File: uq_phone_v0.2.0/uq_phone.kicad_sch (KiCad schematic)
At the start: 0 parts

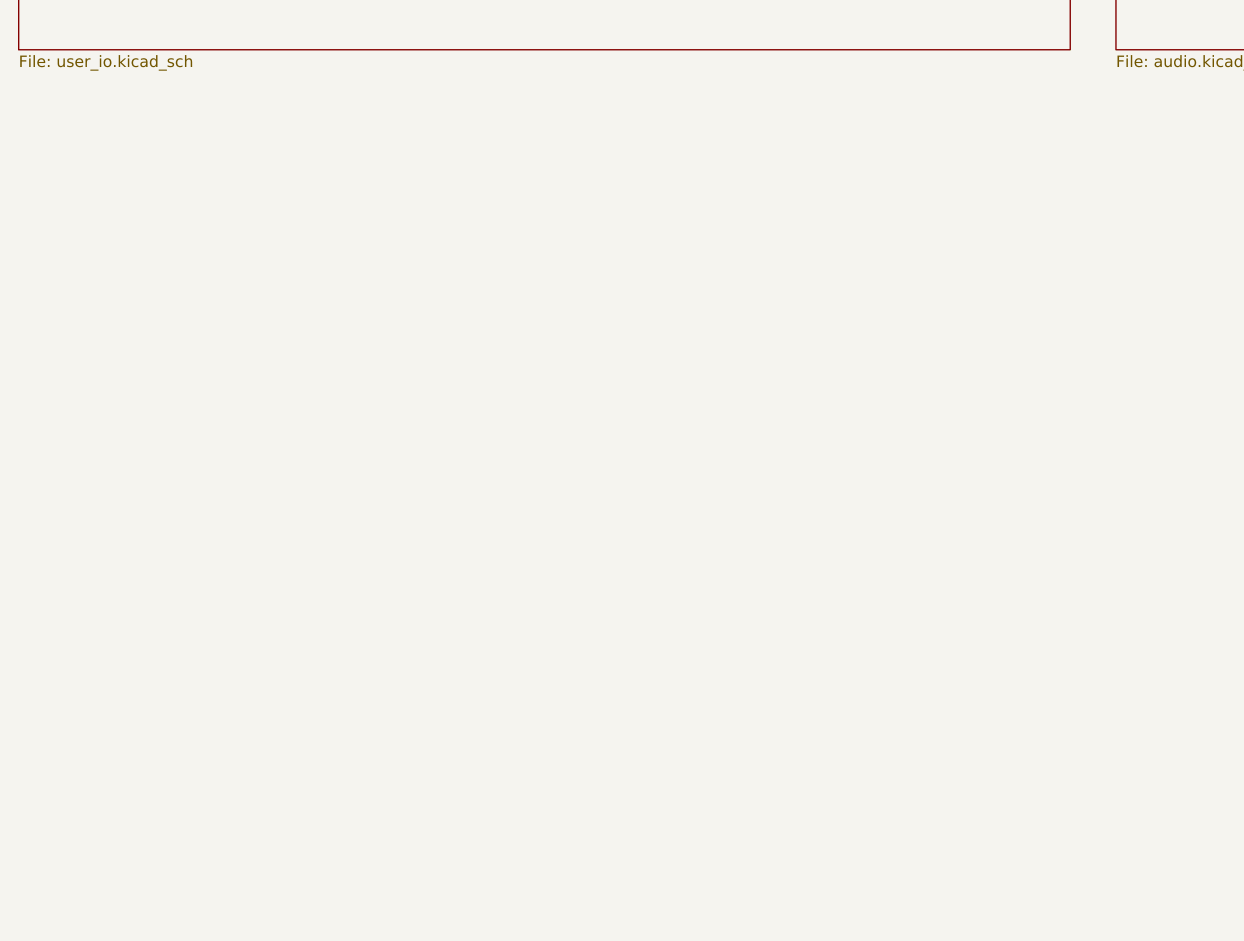
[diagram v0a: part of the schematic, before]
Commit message: Add soft power switch and update PCB design
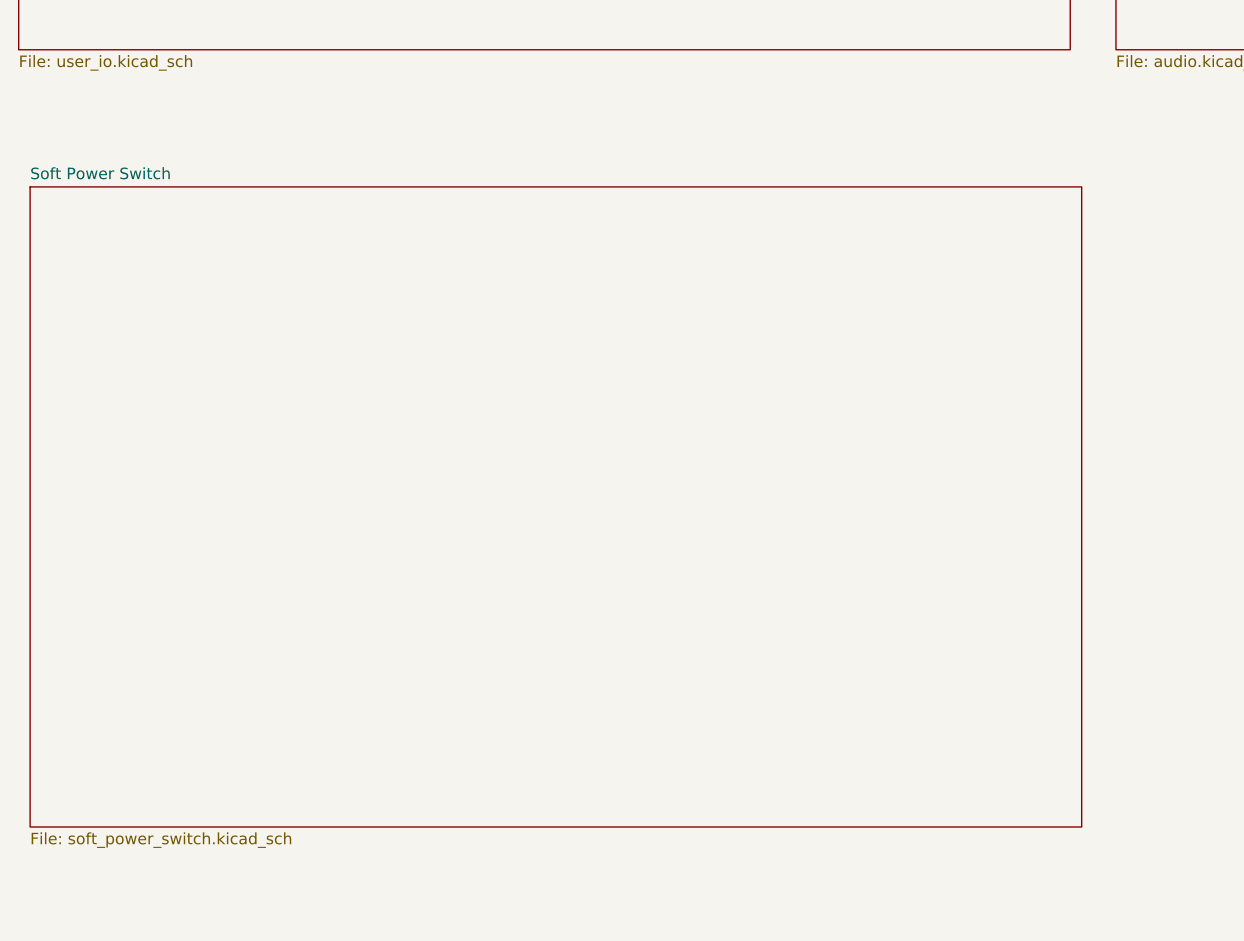
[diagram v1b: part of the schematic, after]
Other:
- added sheet Soft Power Switch (soft_power_switch.kicad_sch)
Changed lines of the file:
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@@
+	)
+	(sheet
+		(at 19.05 180.34)
+		(size 116.84 71.12)
+		(exclude_from_sim no)
+		(in_bom yes)
+		(on_board yes)
+		(dnp no)
+		(fields_autoplaced yes)
+		(stroke
+			(width 0.1524)
+			(type solid)
+		)
+		(fill
+			(color 0 0 0 0.0000)
+		)
+		(property "Sheetname" "Soft Power Switch"
+			(at 19.05 179.6284 0)
+			(effects
+				(font
+					(size 1.27 1.27)
+				)
+				(justify left bottom)
+			)
+		)
+		(property "Sheetfile" "soft_power_switch.kicad_sch"
+			(at 19.05 252.0446 0)
+			(effects
+				(font
+					(size 1.27 1.27)
+				)
+				(justify left top)
+			)
+		)
+		(instances
+			(project "uq_phone"
+				(path "/14f57415-6807-40a5-bb38-3cb818a2cdae"
+					(page "8")
+				)
+			)
+		)
 	)
 	(sheet

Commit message: new display work
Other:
- added sheet Display (display.kicad_sch)
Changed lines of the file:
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@@
+	)
+	(sheet
+		(at 139.7 180.34)
+		(size 115.57 71.12)
+		(exclude_from_sim no)
+		(in_bom yes)
+		(on_board yes)
+		(dnp no)
+		(fields_autoplaced yes)
+		(stroke
+			(width 0.1524)
+			(type solid)
+		)
+		(fill
+			(color 0 0 0 0.0000)
+		)
+		(property "Sheetname" "Display"
+			(at 139.7 179.6284 0)
+			(effects
+				(font
+					(size 1.27 1.27)
+				)
+				(justify left bottom)
+			)
+		)
+		(property "Sheetfile" "display.kicad_sch"
+			(at 139.7 252.0446 0)
+			(effects
+				(font
+					(size 1.27 1.27)
+				)
+				(justify left top)
+			)
+		)
+		(instances
+			(project "uq_phone"
+				(path "/14f57415-6807-40a5-bb38-3cb818a2cdae"
+					(page "9")
+				)
+			)
+		)
 	)
 	(sheet

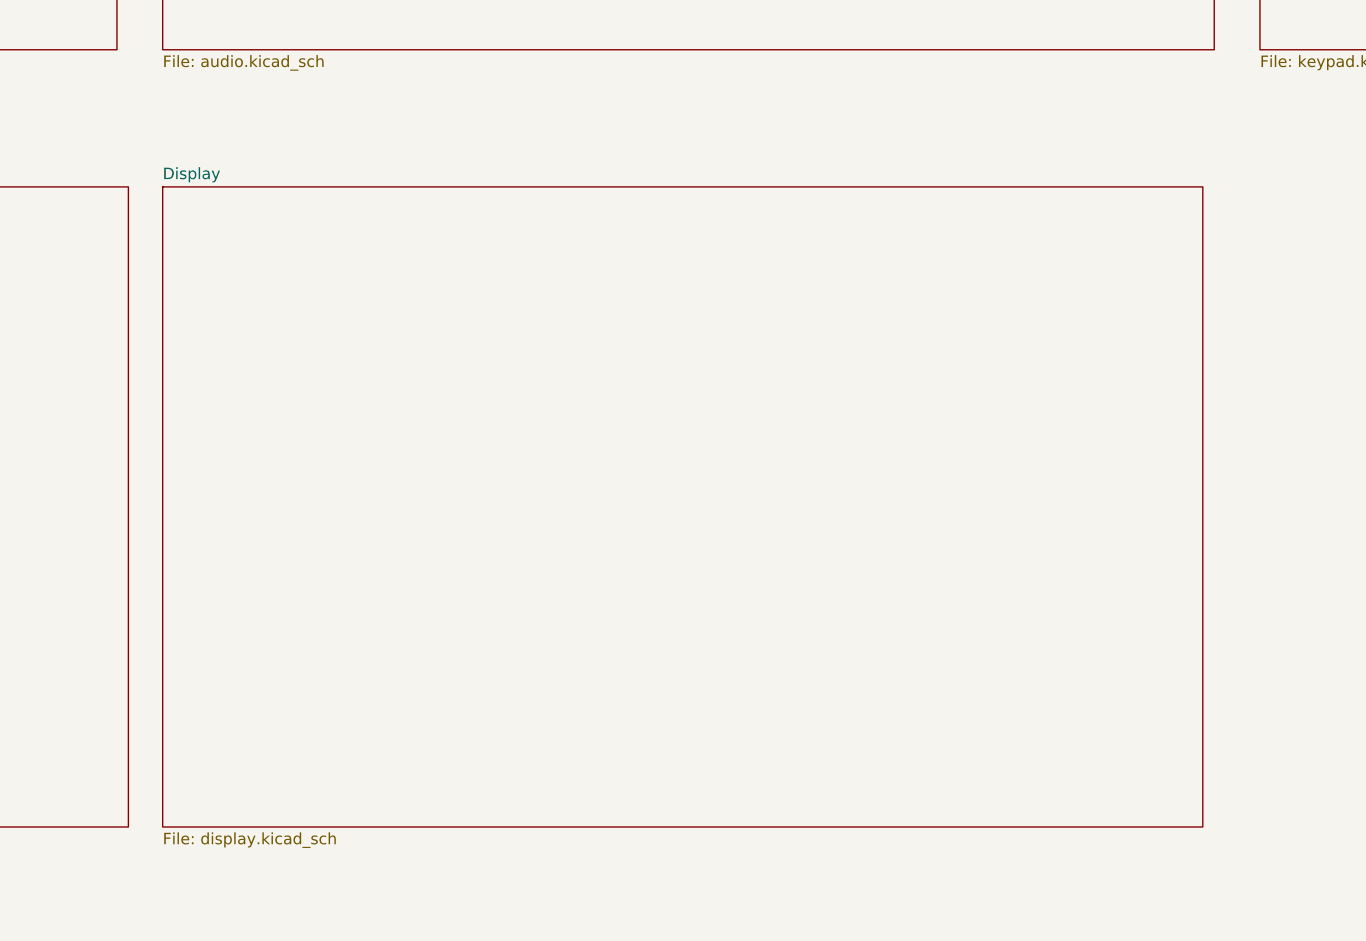
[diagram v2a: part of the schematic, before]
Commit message: Prototype without GPIO expander
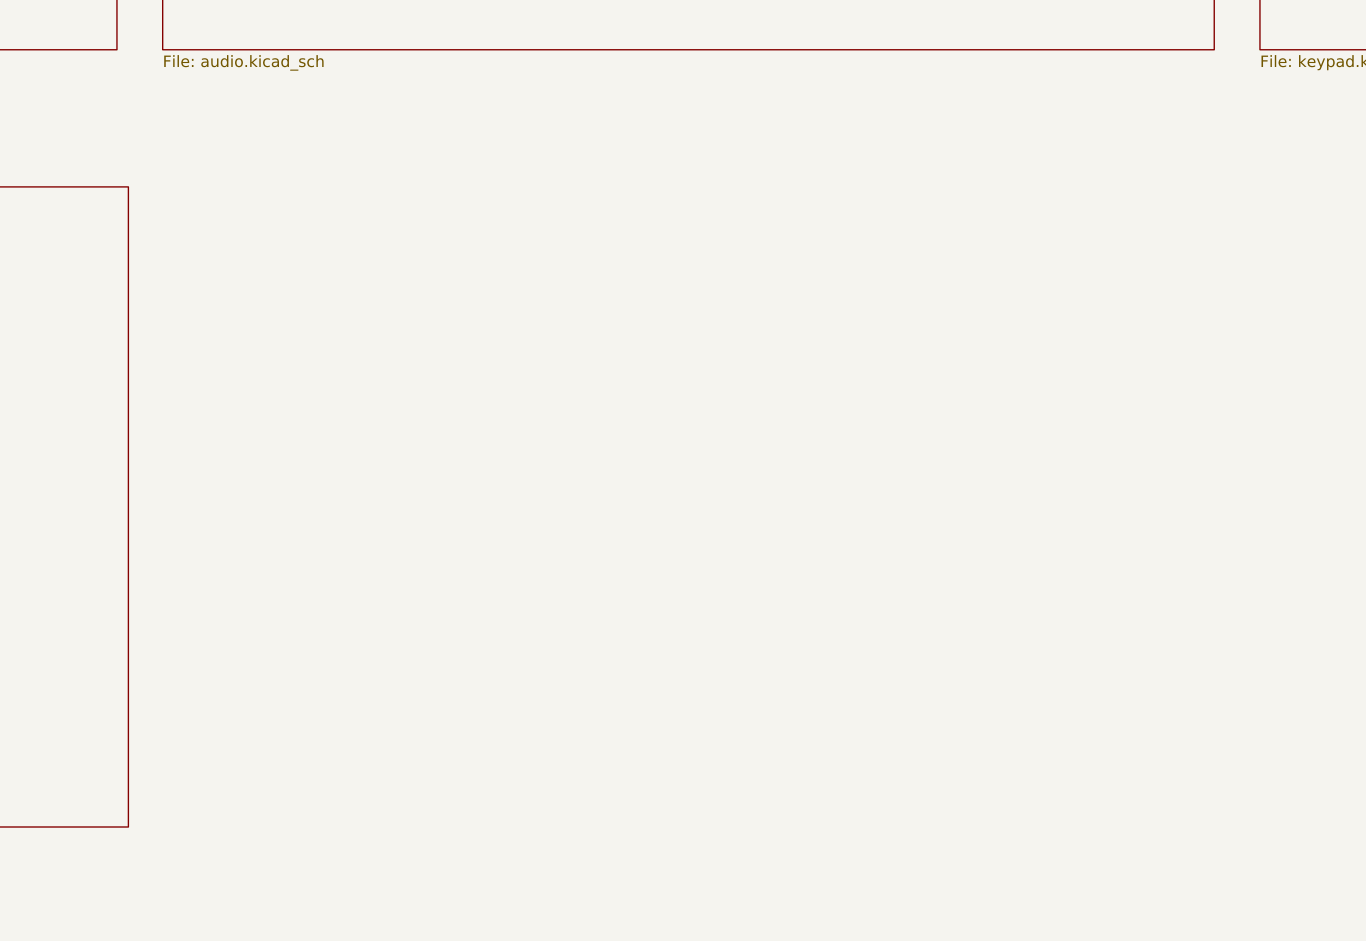
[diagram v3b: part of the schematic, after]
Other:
- removed sheet Display
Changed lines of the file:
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@@
-	)
-	(sheet
-		(at 139.7 180.34)
-		(size 115.57 71.12)
-		(exclude_from_sim no)
-		(in_bom yes)
-		(on_board yes)
-		(dnp no)
-		(fields_autoplaced yes)
-		(stroke
-			(width 0.1524)
-			(type solid)
-		)
-		(fill
-			(color 0 0 0 0.0000)
-		)
-		(property "Sheetname" "Display"
-			(at 139.7 179.6284 0)
-			(effects
-				(font
-					(size 1.27 1.27)
-				)
-				(justify left bottom)
-			)
-		)
-		(property "Sheetfile" "display.kicad_sch"
-			(at 139.7 252.0446 0)
-			(effects
-				(font
-					(size 1.27 1.27)
-				)
-				(justify left top)
-			)
-		)
-		(instances
-			(project "uq_phone"
-				(path "/14f57415-6807-40a5-bb38-3cb818a2cdae"
-					(page "9")
-				)
-			)
-		)
 	)
 	(sheet

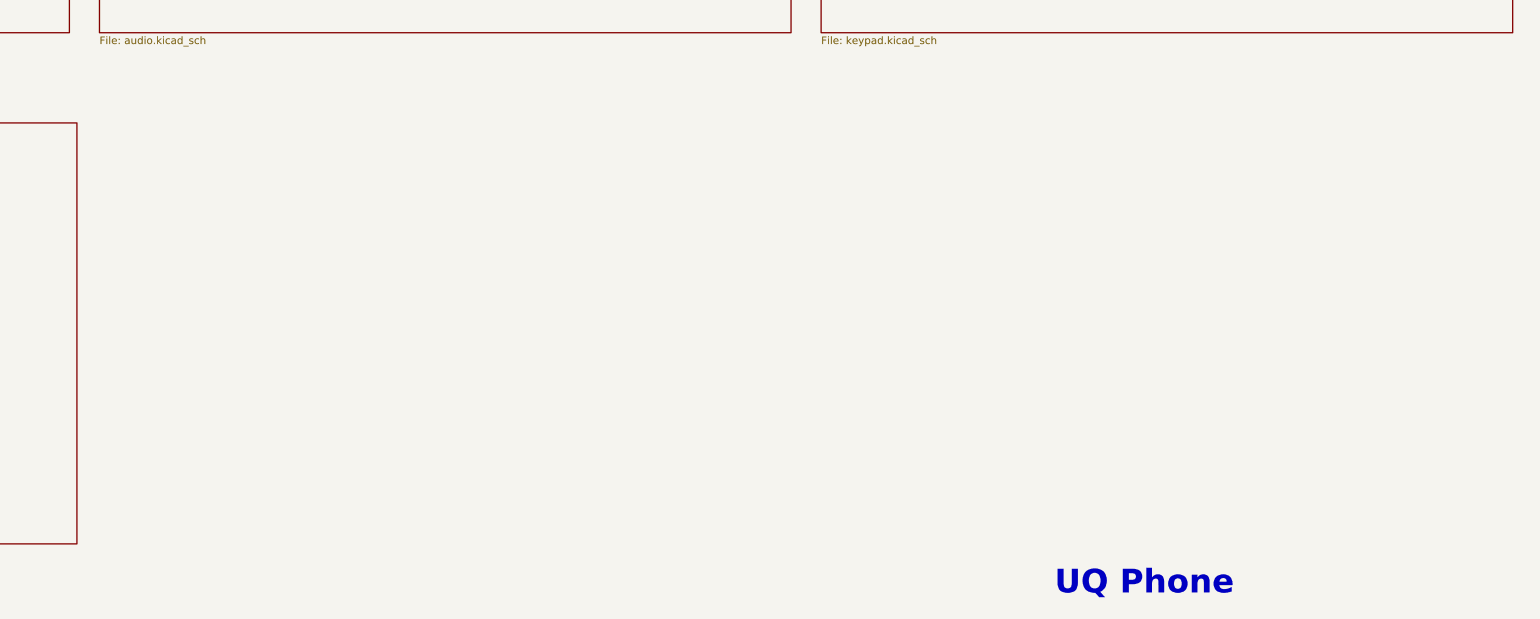
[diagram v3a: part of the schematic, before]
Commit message: Add GPIO expander and 16-bit FMC display schematic
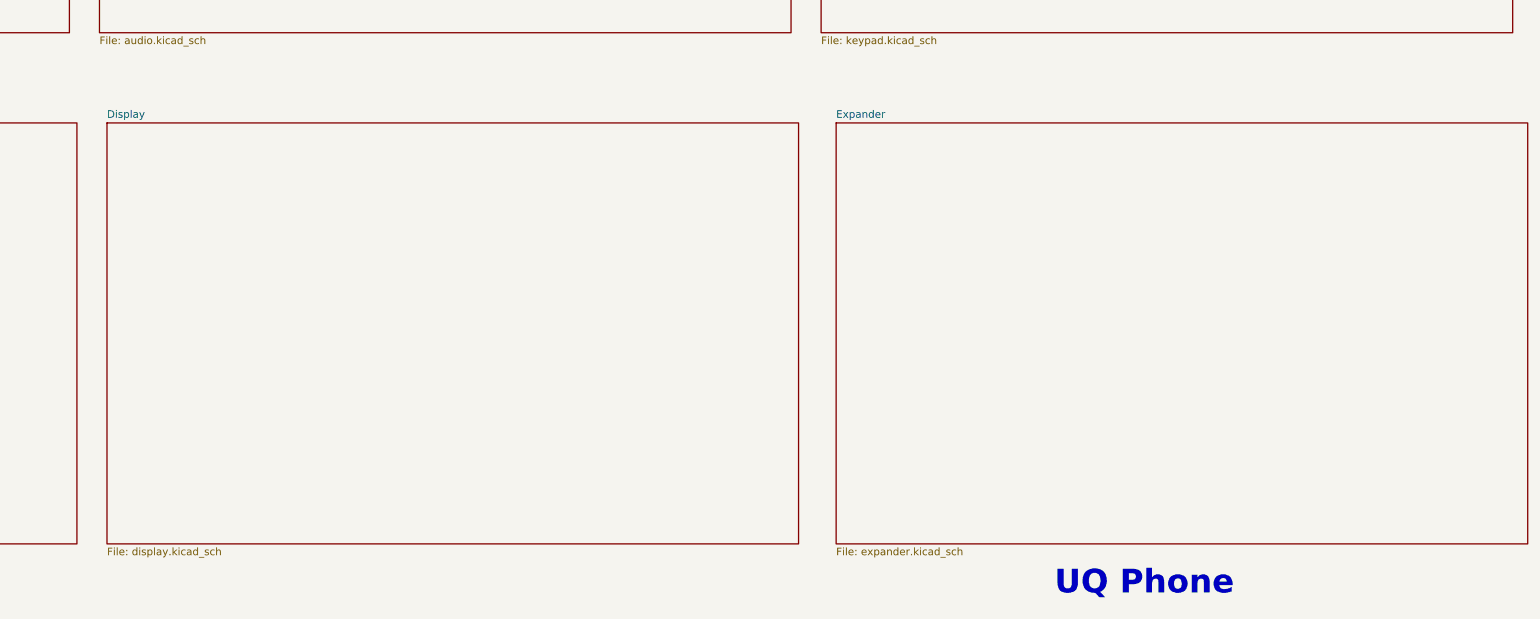
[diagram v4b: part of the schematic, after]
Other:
- added sheet Display (display.kicad_sch)
- added sheet Expander (expander.kicad_sch)
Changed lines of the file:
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@@
+	)
+	(sheet
+		(at 140.97 180.34)
+		(size 116.84 71.12)
+		(exclude_from_sim no)
+		(in_bom yes)
+		(on_board yes)
+		(dnp no)
+		(fields_autoplaced yes)
+		(stroke
+			(width 0.1524)
+			(type solid)
+		)
+		(fill
+			(color 0 0 0 0.0000)
+		)
+		(property "Sheetname" "Display"
+			(at 140.97 179.6284 0)
+			(effects
+				(font
+					(size 1.27 1.27)
+				)
+				(justify left bottom)
+			)
+		)
+		(property "Sheetfile" "display.kicad_sch"
+			(at 140.97 252.0446 0)
+			(effects
+				(font
+					(size 1.27 1.27)
+				)
+				(justify left top)
+			)
+		)
+		(instances
+			(project "uq_phone"
+				(path "/14f57415-6807-40a5-bb38-3cb818a2cdae"
+					(page "9")
+				)
+			)
+		)
 	)
 	(sheet
@@
 				)
 			)
+		)
+	)
+	(sheet
+		(at 264.16 180.34)
+		(size 116.84 71.12)
+		(exclude_from_sim no)
+		(in_bom yes)
+		(on_board yes)
+		(dnp no)
+		(fields_autoplaced yes)
+		(stroke
+			(width 0.1524)
+			(type solid)
+		)
+		(fill
+			(color 0 0 0 0.0000)
+		)
+		(property "Sheetname" "Expander"
+			(at 264.16 179.6284 0)
+			(effects
+				(font
+					(size 1.27 1.27)
+				)
+				(justify left bottom)
+			)
+		)
+		(property "Sheetfile" "expander.kicad_sch"
+			(at 264.16 252.0446 0)
+			(effects
+				(font
+					(size 1.27 1.27)
+				)
+				(justify left top)
+			)
+		)
+		(instances
+			(project "uq_phone"
+				(path "/14f57415-6807-40a5-bb38-3cb818a2cdae"
+					(page "10")
+				)
+			)
